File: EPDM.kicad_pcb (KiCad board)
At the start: 2 copper layers, 31.4 x 26.9 mm, 25 parts, among them J1 Conn_01x34_MountingPin, J2 Conn_01x24_MountingPin, J3 Conn_01x09_Female, J4 Conn_01x10, J5 Conn_01x10, Q1 IRLML6344

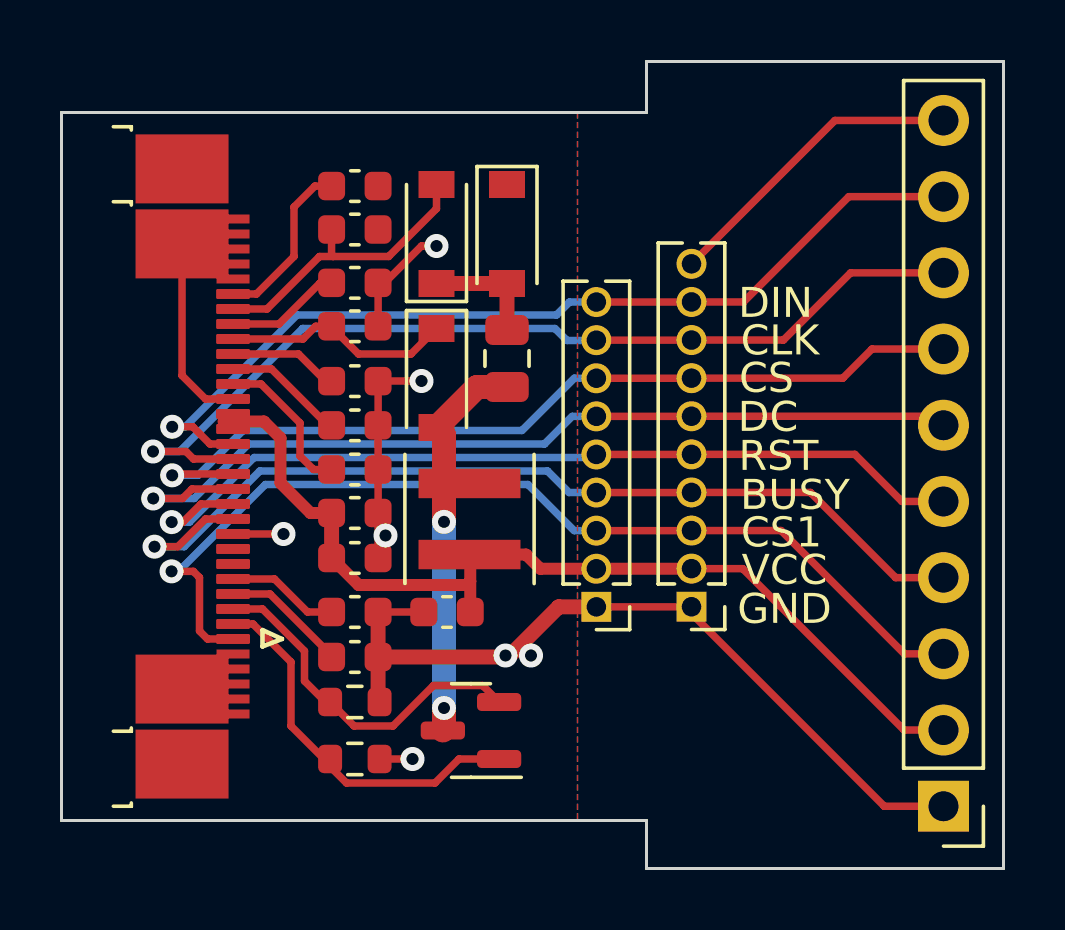
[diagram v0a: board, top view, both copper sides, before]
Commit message: Rotate some of components
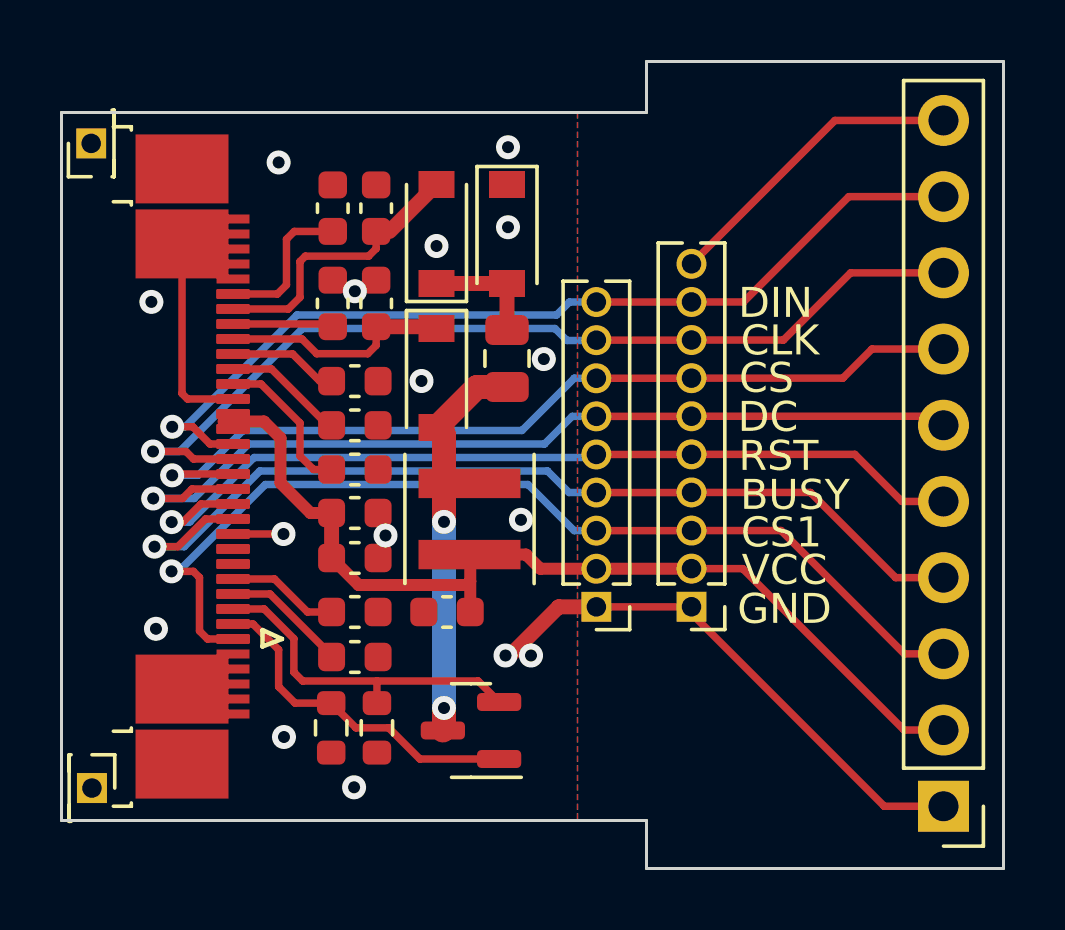
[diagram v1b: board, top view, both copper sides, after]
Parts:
- added REF**: PinHeader_1x01_P1.27mm_Vertical, Connector_PinHeader_1.27mm:PinHeader_1x01_P1.27mm_Vertical, F.Cu at (120.0, 76.5)
- added REF**: PinHeader_1x01_P1.27mm_Vertical, Connector_PinHeader_1.27mm:PinHeader_1x01_P1.27mm_Vertical, F.Cu at (120.0, 98.0)
- moved R1 1.30 mm to (128.0, 96.0), turned to -90 degrees
- moved R2 1.13 mm to (129.5, 96.0), turned to -90 degrees
- moved C6 1.04 mm to (129.5, 81.9), turned to 90 degrees
- moved C11 1.04 mm to (128.0, 78.7), turned to 90 degrees
- moved C10 1.01 mm to (128.0, 81.9), turned to 90 degrees
- moved C8 1.01 mm to (129.5, 78.7), turned to 90 degrees
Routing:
- net GND: track 47.4 -> 26.7 mm, vias 7 -> 16
- net /GDR: track 12.8 -> 11.5 mm
- net /VCOM: track 5.74 -> 5.08 mm
- net /VSL: track 3.85 -> 3.26 mm

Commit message: Size optimization
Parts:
- removed C7: 1uF/25V, Capacitor_SMD:C_0603_1608Metric
- removed REF** (x2): PinHeader_1x01_P1.27mm_Vertical, Connector_PinHeader_1.27mm:PinHeader_1x01_P1.27mm_Vertical
- C12: footprint Capacitor_SMD:C_0603_1608Metric -> Capacitor_SMD:C_0805_2012Metric
- moved C3 1.58 mm to (128.8, 92.1)
- moved R1 1.55 mm to (128.0, 94.5), turned to 90 degrees
- moved R2 1.55 mm to (129.5, 94.5)
- moved C2 1.52 mm to (128.8, 90.6)
- moved C4 1.48 mm to (128.8, 88.9)
- moved C5 1.47 mm to (128.8, 85.9)
- moved C1 1.45 mm to (128.8, 87.4)
- moved Q1 1.20 mm to (132.2, 95.0)
- moved J1 0.48 mm to (123.9, 87.3)
- moved J2 0.48 mm to (123.9, 87.3)
- moved C12 0.22 mm to (132.0, 92.3)
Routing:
- net /VPP: track 4.06 -> 0.00 mm
- net /RESE: track 11.5 -> 9.48 mm
- net /VDD: track 5.11 -> 3.37 mm
- net +3V3: track 32.4 -> 30.8 mm
- net /VGL: track 4.18 -> 3.02 mm
- net /GDR: track 11.5 -> 10.3 mm
- net Net-(C13-Pad1): track 13.1 -> 12.3 mm
- net /VGH: track 3.74 -> 2.98 mm
- net /PREVGL: track 9.54 -> 8.93 mm
- net GND: track 26.7 -> 26.1 mm, vias 16 -> 22
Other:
- board size 31.4 x 26.9 mm -> 30.8 x 26.9 mm
- board text added: "V0.2"
- board text added: "^"
